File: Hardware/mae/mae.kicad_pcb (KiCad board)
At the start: 2 copper layers, 79 x 39.5 mm, 34 parts, among them Q1 Q_NJFET_DSG, U4 NE5532

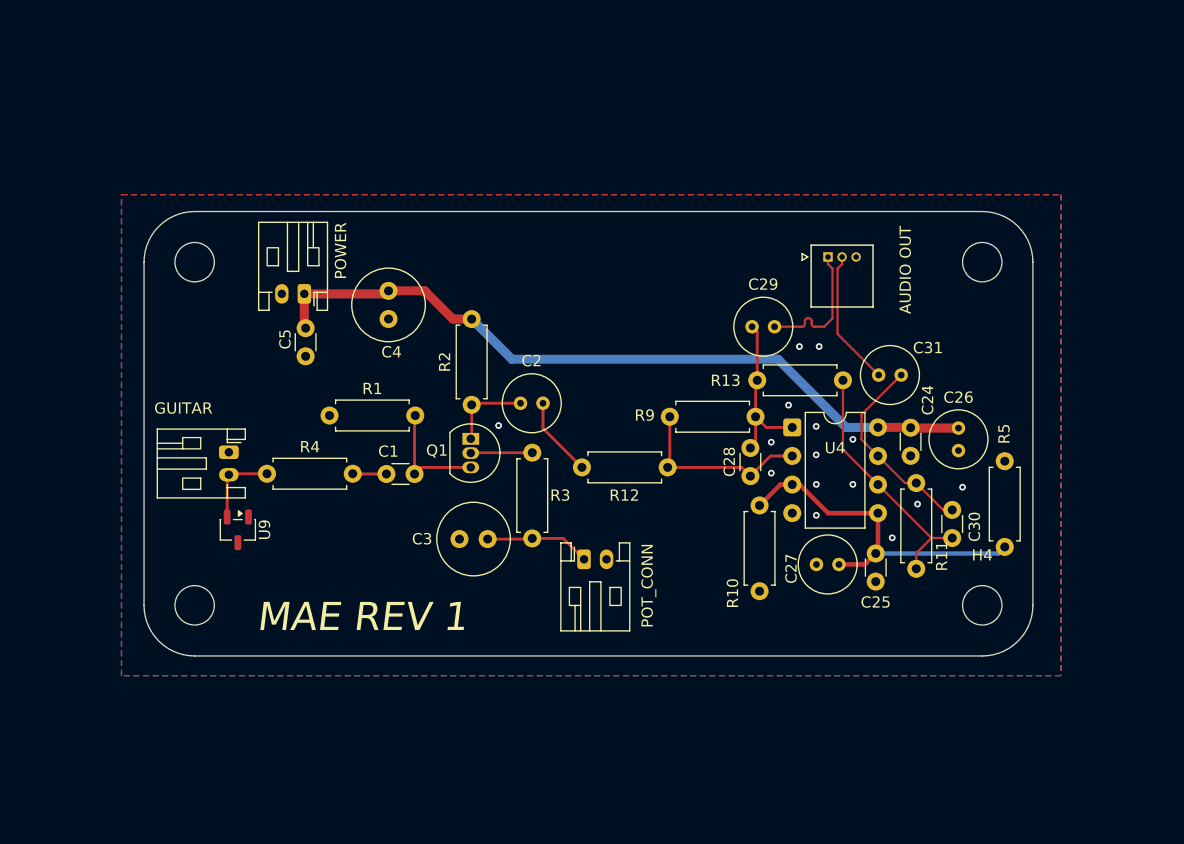
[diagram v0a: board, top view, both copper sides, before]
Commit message: Mae: stiching vias added
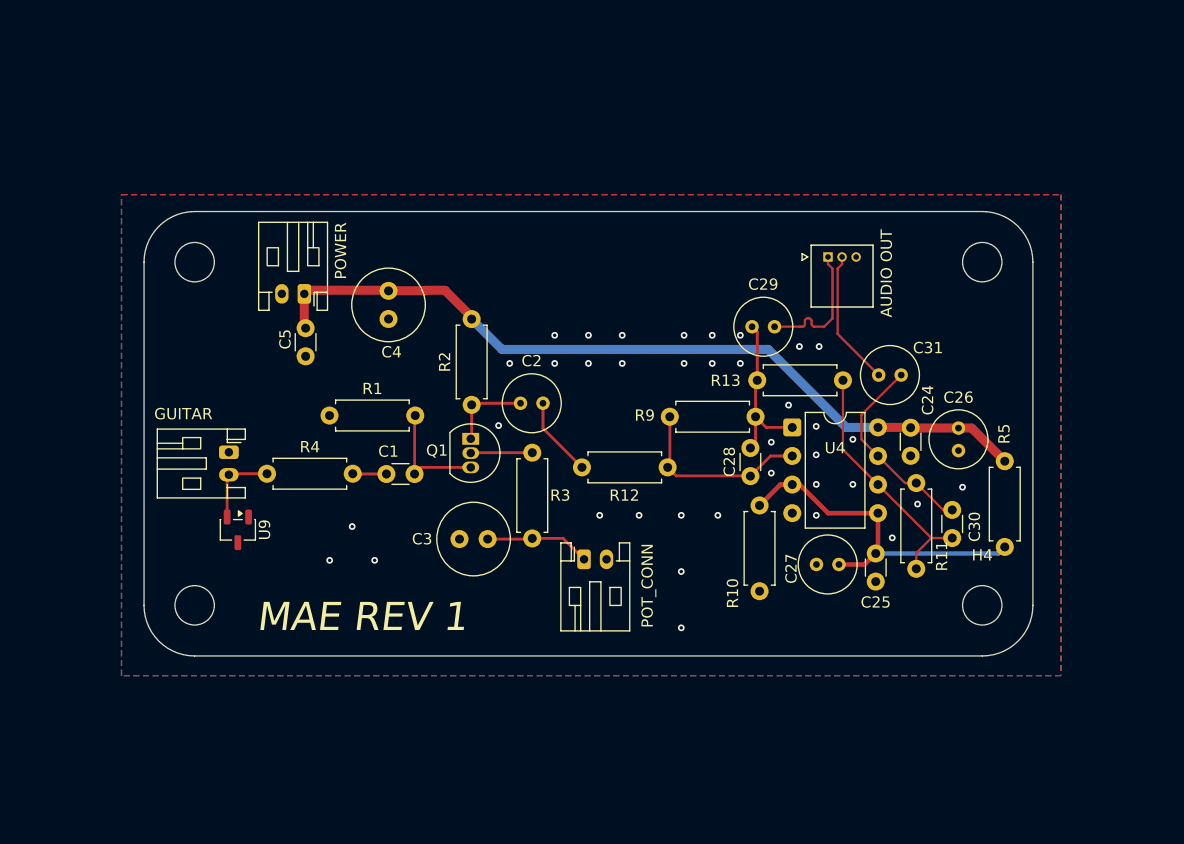
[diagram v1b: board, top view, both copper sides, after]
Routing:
- net +9V: track 66.4 -> 71.9 mm
- net GND: vias 15 -> 37

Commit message: Mae: polarised caps, new layout and prints
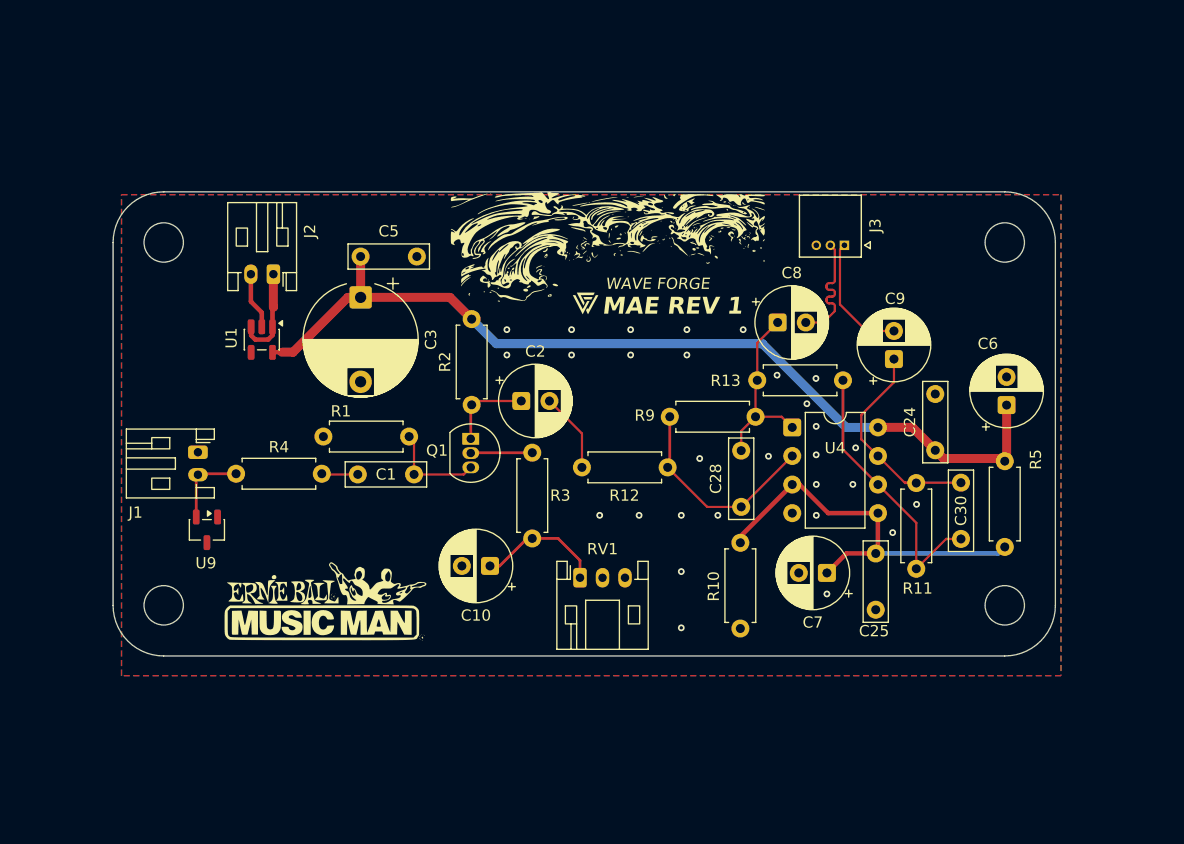
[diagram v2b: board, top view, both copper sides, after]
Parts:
- removed C26, C27, C29, C31: 10uF, Capacitor_THT:C_Radial_D5.0mm_H5.0mm_P2.00mm
- removed C4: 100uF, Capacitor_THT:C_Radial_D6.3mm_H7.0mm_P2.50mm
- added C10: c, Capacitor_THT:CP_Radial_D6.3mm_P2.50mm, F.Cu at (126.2, 119.5)
- added C6: 10uF, Capacitor_THT:CP_Radial_D6.3mm_P2.50mm, F.Cu at (172.2, 105.2)
- added C7: 10uF, Capacitor_THT:CP_Radial_D6.3mm_P2.50mm, F.Cu at (156.2, 120.1)
- added C8: 10uF, Capacitor_THT:CP_Radial_D6.3mm_P2.50mm, F.Cu at (151.8, 97.9)
- added C9: 10uF, Capacitor_THT:CP_Radial_D6.3mm_P2.50mm, F.Cu at (162.2, 101.1)
- added G***: LOGO, my footprints:waves, F.Cu at (136.7, 92.8)
- added G***: LOGO, MyFootprints:logo, F.Cu at (134.5, 95.1)
- added G***: LOGO, my footpritns:musicman, F.Cu at (111.8, 123.2)
- added U1: MAX40200AUK, Package_TO_SOT_SMD:SOT-23-5, F.Cu at (106.0, 99.4)
- C1, C24, C25, C28, C30, C5: footprint Capacitor_THT:C_Disc_D3.0mm_W1.6mm_P2.50mm -> Capacitor_THT:C_Rect_L7.0mm_W2.0mm_P5.00mm
- C2: footprint Capacitor_THT:C_Radial_D5.0mm_H5.0mm_P2.00mm -> Capacitor_THT:CP_Radial_D6.3mm_P2.50mm
- C3: value C -> 100uF; footprint Capacitor_THT:C_Radial_D6.3mm_H7.0mm_P2.50mm -> Capacitor_THT:CP_Radial_D10.0mm_P7.50mm
- J3: renamed from AUDIO OUT
- RV1: renamed from POT_CONN; footprint Connector_JST:JST_PH_S2B-PH-K_1x02_P2.00mm_Horizontal -> Connector_JST:JST_PH_S3B-PH-K_1x03_P2.00mm_Horizontal
- moved C3 23.2 mm to (114.8, 95.6), turned to -90 degrees
- moved C5 8.03 mm to (114.8, 92.0), turned to 0 degrees
- moved R10 3.73 mm to (148.5, 125.1)
- moved H3 3.26 mm to (97.2, 90.8)
- moved J2 3.26 mm to (107.0, 93.6)
- moved C24 2.97 mm to (165.8, 109.2), turned to 90 degrees
- moved C28 2.85 mm to (148.6, 114.2)
- moved H6 2.75 mm to (97.2, 123.0)
- moved J1 2.75 mm to (100.3, 109.4)
- moved R4 2.75 mm to (103.7, 111.3)
- moved U9 2.75 mm to (101.1, 116.3)
- moved H5 2.66 mm to (172.0, 90.8)
- moved C1 2.54 mm to (114.5, 111.4)
- moved H4 2.00 mm to (172.0, 123.0)
- moved R1 1.95 mm to (111.4, 108.0)
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- renumbered GUITAR to J1, POWER to J2
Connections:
- C3 pad 1: GND -> +9V
- C3 pad 2: Net-(C3-Pad2) -> GND
- J2 pad 1: +9V -> Net-(J2-Pin_1)
- J3 pad 1: /AUDIO_OUT+ -> /AUDIO_OUT-
- J3 pad 2: /AUDIO_OUT- -> /AUDIO_OUT+
- R3 pad 1: Net-(C3-Pad2) -> Net-(C10-Pad1)
- RV1 pad 1: Net-(C3-Pad2) -> Net-(C10-Pad1)
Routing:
- net Net-(C10-Pad1): track 0.00 -> 11.4 mm
- net +9V: track 71.9 -> 82.0 mm
- net Net-(C3-Pad2): track 9.36 -> 0.00 mm
- net Net-(J2-Pin_1): track 0.00 -> 8.44 mm
- net GND: track 0.00 -> 5.08 mm, vias 37 -> 29
- net /VBIAS: track 31.4 -> 36.2 mm
- net Net-(U4A--): track 16.7 -> 19.3 mm
- net Net-(U4B--): track 22.4 -> 24.5 mm
- net Net-(C30-Pad2): track 17.8 -> 19.8 mm
- net /GATE: track 10.5 -> 8.84 mm
- net /U4A_AUDIO: track 14.9 -> 16.1 mm
- net /AUDIO_OUT+: track 12.1 -> 11.1 mm
- net /AUDIO_OUT-: track 12.2 -> 11.2 mm
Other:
- board size 79 x 39.5 mm -> 83.8 x 41.2 mm
- board text added: "WAVE FORGE"

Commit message: Gen: PSU, rev 1 schems done, mae and shori orderd
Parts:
- added G***: LOGO, my footpritns:majesty, F.Cu at (97.5, 100.2)
- AUDIO OUT: renamed from J3
- C3: footprint Capacitor_THT:CP_Radial_D10.0mm_P7.50mm -> Capacitor_THT:CP_Radial_D10.0mm_P5.00mm
- GUITAR IN: renamed from J1
- moved C3 2.00 mm to (114.8, 97.6)
- moved C5 0.75 mm to (114.8, 92.8)
- renumbered J2 to POWER, RV1 to TEXTURE

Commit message: New Gallery Images for Reddit
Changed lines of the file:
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@@
 		(polygon
 			(pts
-				(xy 93.5 86.5) (xy 177 86.5) (xy 177 129.25) (xy 93.5 129.25)
+				(xy 84.7 71.2) (xy 185.95 76.15) (xy 185.95 136.2) (xy 84.85 142.25)
 			)
 		)
